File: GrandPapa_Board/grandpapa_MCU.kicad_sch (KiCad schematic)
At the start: 15 parts, among them J6 Conn_02x06, U8 PIC18F26K83, Y1 12MHz

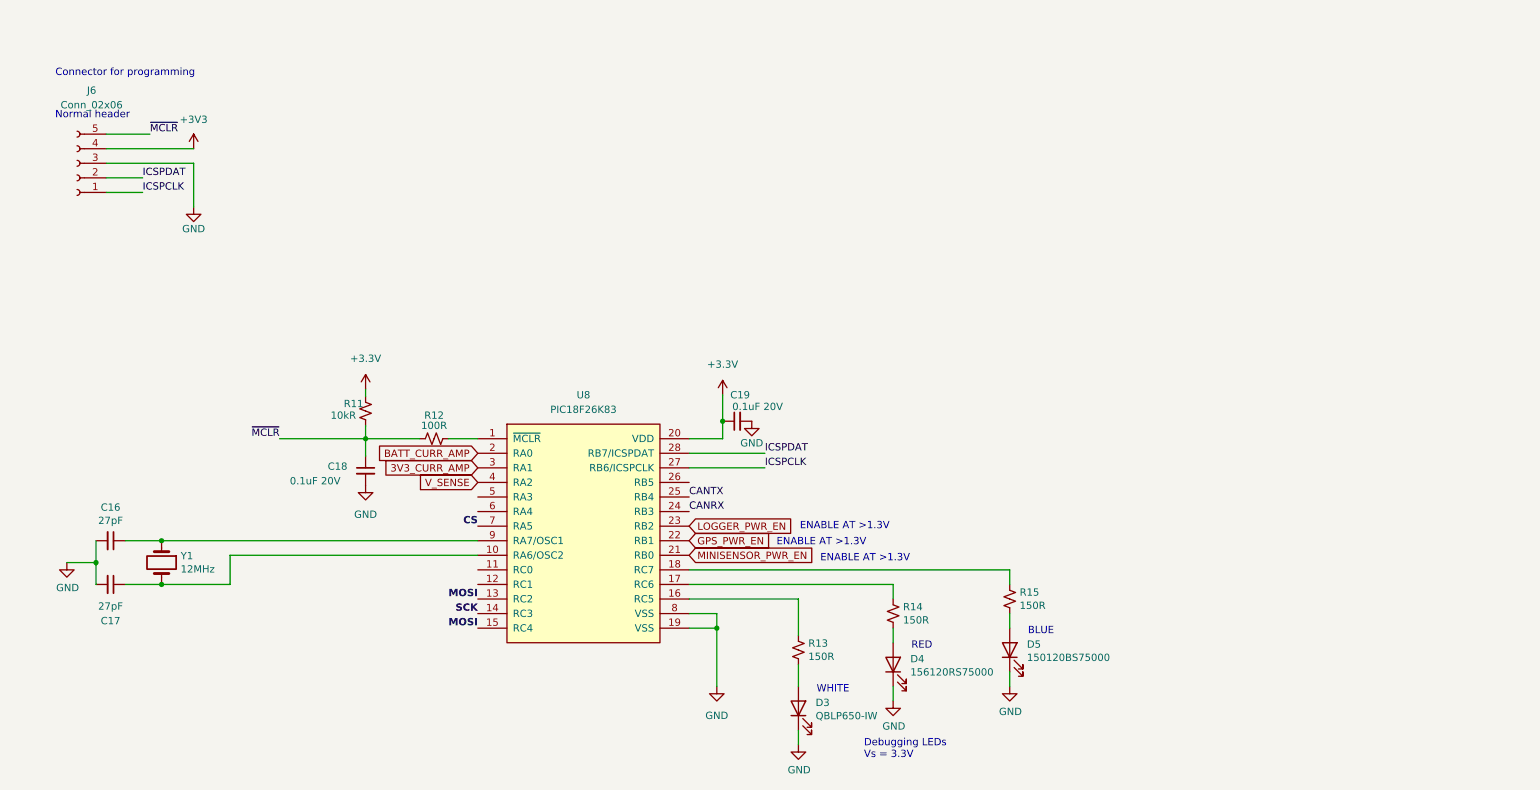
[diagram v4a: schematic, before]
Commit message: Add MCP2515, MCU pin naming scheme
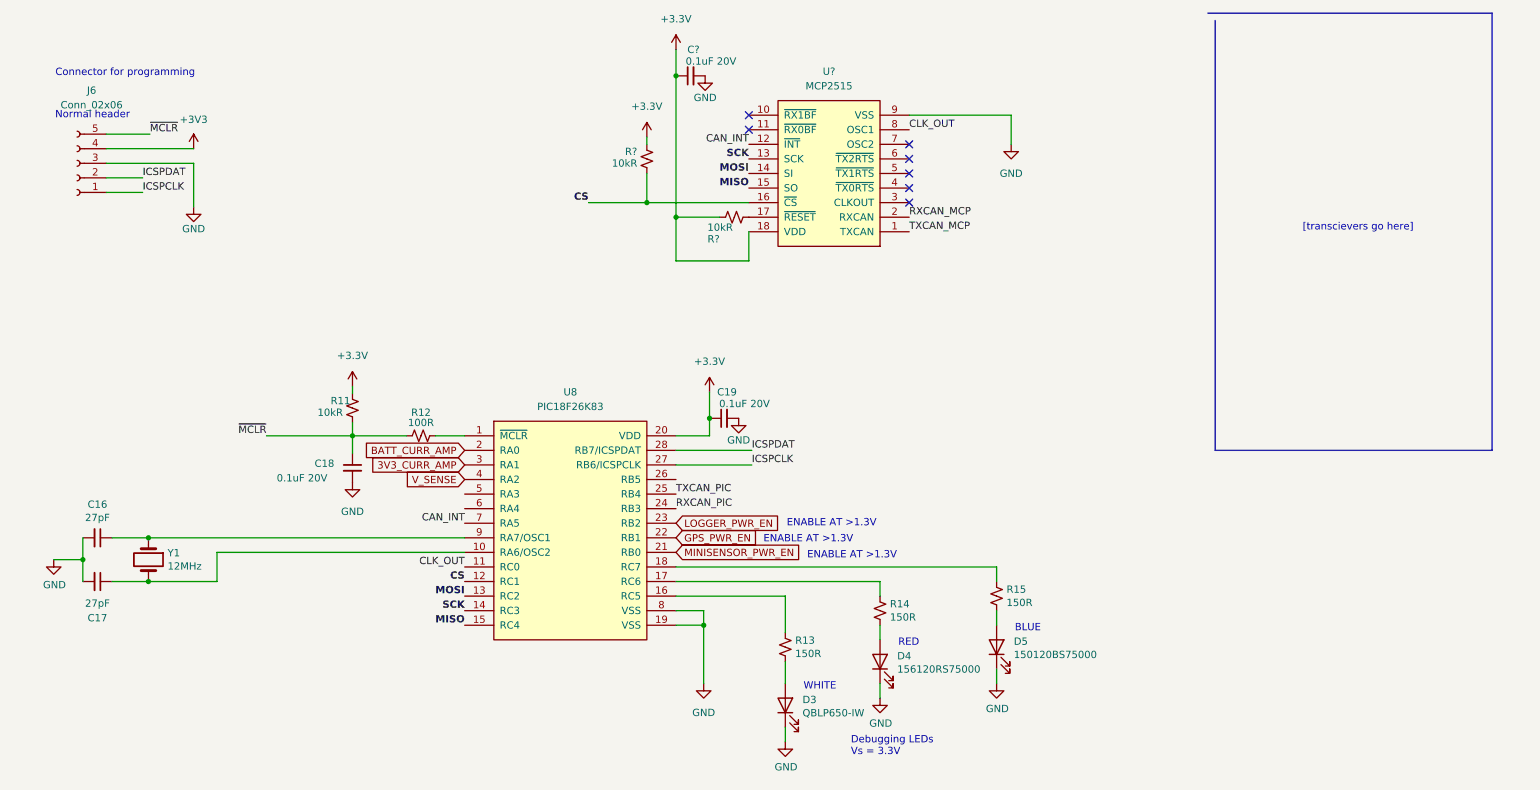
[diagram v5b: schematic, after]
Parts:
- added C?: 0.1uF 20V, symbol Device:C_Small
- added R? (x2): 10kR, symbol Device:R_Small_US
- added U?: MCP2515, symbol CANHW:MCP2515
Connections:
- net +3V3: now also C?.1, R?.1, R?.1, U?.18 (VDD)
- net CS: now also U8.12 (RC1), R?.2, U?.16 (~{CS}); no longer U8.7 (RA5)
- net GND: now also C?.2, U?.9 (VSS)
- net MOSI: now also U?.14 (SI); no longer U8.15 (RC4)
- net SCK: now also U?.13 (SCK)
- net CLK_OUT: now reaches U8.11 (RC0)
- net CLK_OUT: now also U?.8 (OSC1)
- net CANRX renamed RXCAN_PIC
- net CANTX renamed TXCAN_PIC
- new net: R?.2, U?.17 (~{RESET})
- new net CAN_INT: U8.7 (RA5), U?.12 (~{INT})
- new net MISO: U8.15 (RC4), U?.15 (SO)
- new net RXCAN_MCP: U?.2 (RXCAN)
- new net TXCAN_MCP: U?.1 (TXCAN)
- no-connect marks 0 -> 7
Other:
- note added: "[transcievers go here]"
- moved on the sheet: C16, C17, C18, C19, D3, D4, D5, R11, R12, R13, R14, R15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

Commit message: Add INA180 to symbol lib, update 5v switch labels
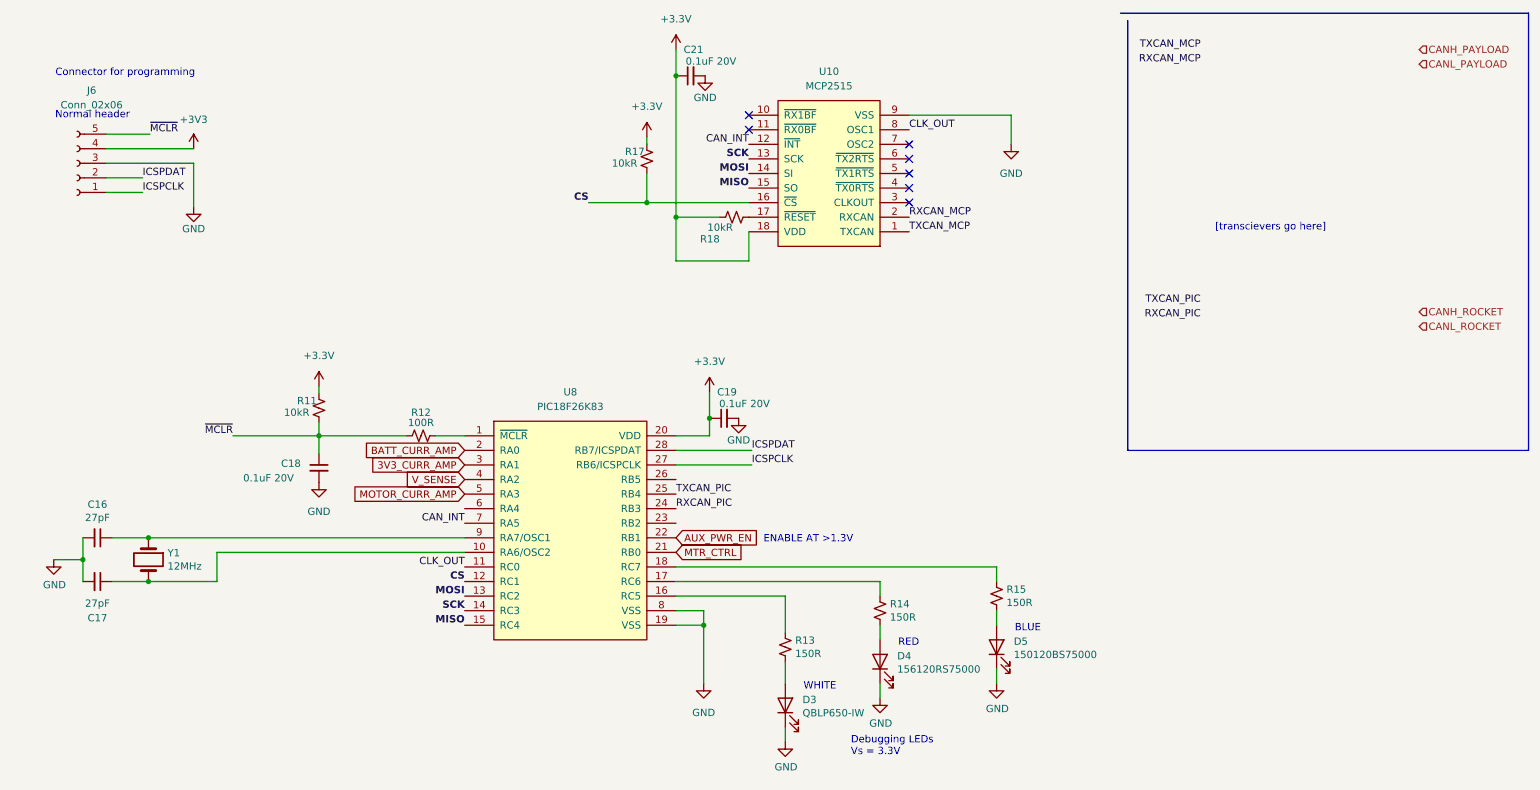
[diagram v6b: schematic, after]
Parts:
- gave numbers to parts that had none: 4
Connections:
- net MOTOR_CURR_AMP: now reaches U8.5 (RA3)
- net GPS_PWR_EN renamed AUX_PWR_EN
- net LOGGER_PWR_EN: no longer names the net of U8.23 (RB2)
- net MINISENSOR_PWR_EN renamed MTR_CTRL
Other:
- moved on the sheet: C18, R11
